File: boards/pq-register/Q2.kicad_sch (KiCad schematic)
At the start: 94 parts, among them Q100 MMBT5401, Q65 MMBT5401, Q73 MMBT5401, Q74 MMBT5401, Q75 MMBT5401, Q76 MMBT5401, Q77 MMBT5401, Q78 MMBT5401, Q79 MMBT5401, Q80 MMBT5401, Q81 MMBT5401, Q82 MMBT5401

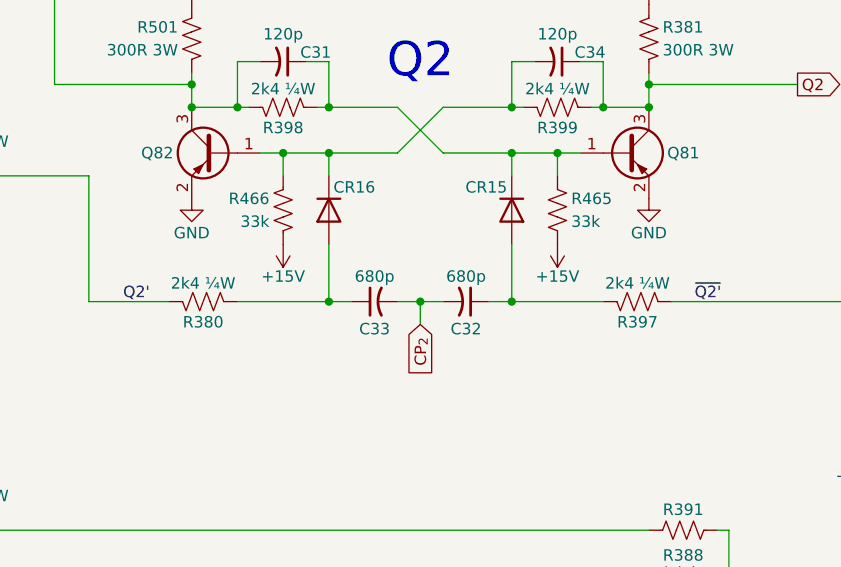
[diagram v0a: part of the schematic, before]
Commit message: Route resistors in the second column.
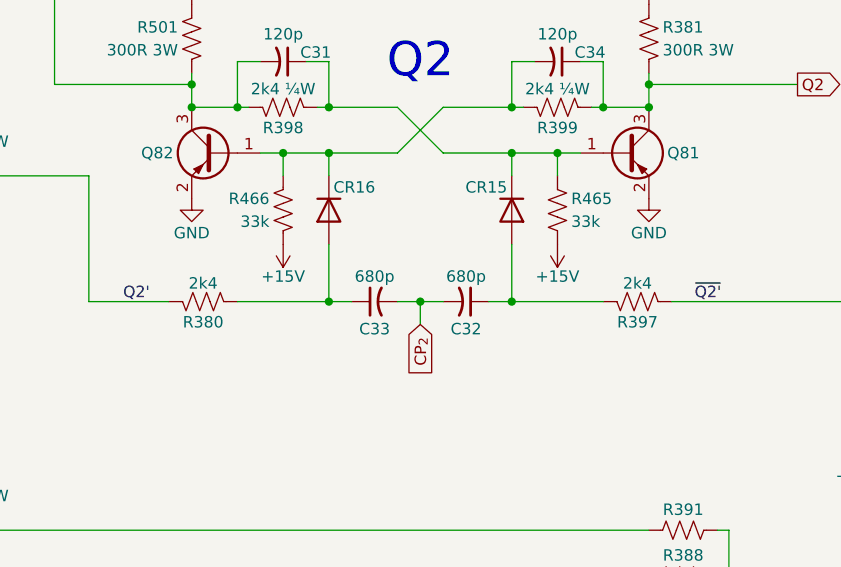
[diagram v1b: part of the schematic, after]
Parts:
- R380, R397: value 2k4 ¼W -> 2k4; footprint Resistor_SMD:R_0603_1608Metric -> Resistor_SMD:R_0402_1005Metric
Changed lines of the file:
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@@
 			)
 		)
-		(property "Value" "2k4 ¼W"
+		(property "Value" "2k4"
 			(at 176.53 61.468 90)
 			(show_name no)
@@
 			)
 		)
-		(property "Footprint" "Resistor_SMD:R_0603_1608Metric"
+		(property "Footprint" "Resistor_SMD:R_0402_1005Metric"
 			(at 176.784 64.516 90)
 			(hide yes)
@@
 			)
 		)
-		(property "Value" "2k4 ¼W"
+		(property "Value" "2k4"
 			(at 224.79 61.468 90)
 			(show_name no)
@@
 			)
 		)
-		(property "Footprint" "Resistor_SMD:R_0603_1608Metric"
+		(property "Footprint" "Resistor_SMD:R_0402_1005Metric"
 			(at 225.044 64.516 90)
 			(hide yes)

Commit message: Route passives in the rightmost column.
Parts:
- R903: renamed from R507; now fitted
- R904: renamed from R508; now fitted
- R906: renamed from R509; now fitted
- R907: renamed from R510; now fitted
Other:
- note removed: "Used 41 & up when IO Key, Data I/O, or A&D Converter boards are used. Works in normal not in 1op mode."
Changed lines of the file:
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@@
 		(comment 1 "https://github.com/Elemecca/lgp21-mini")
 	)
-	(text "Used 41 & up when IO Key,\nData I/O, or A&D Converter\nboards are used. Works in\nnormal not in 1op mode."
-		(exclude_from_sim no)
-		(at 116.078 30.226 0)
-		(effects
-			(font
-				(size 1.27 1.27)
-			)
-			(justify left)
-		)
-	)
 	(text "Q2"
 		(exclude_from_sim no)
@@
 		)
 	)
-	(polyline
-		(pts
-			(xy 118.11 44.45) (xy 118.11 45.72)
-		)
-		(stroke
-			(width 0)
-			(type default)
-		)
-	)
 	(wire
 		(pts
@@
 		)
 	)
-	(polyline
-		(pts
-			(xy 111.76 27.94) (xy 115.57 27.94)
-		)
-		(stroke
-			(width 0)
-			(type default)
-		)
-	)
 	(wire
 		(pts
@@
 		)
 	)
-	(polyline
-		(pts
-			(xy 118.11 44.45) (xy 118.11 45.72)
-		)
-		(stroke
-			(width 0)
-			(type default)
-		)
-	)
 	(wire
 		(pts
@@
 		)
 	)
-	(polyline
-		(pts
-			(xy 111.76 39.37) (xy 118.11 45.72)
-		)
-		(stroke
-			(width 0)
-			(type default)
-		)
-	)
 	(wire
 		(pts
@@
 		)
 	)
-	(polyline
-		(pts
-			(xy 111.76 27.94) (xy 111.76 39.37)
-		)
-		(stroke
-			(width 0)
-			(type default)
-		)
-	)
 	(wire
 		(pts
@@
 		)
 	)
-	(polyline
-		(pts
-			(xy 116.84 45.72) (xy 118.11 45.72)
-		)
-		(stroke
-			(width 0)
-			(type default)
-		)
-	)
 	(wire
 		(pts
@@
 		(on_board yes)
 		(in_pos_files yes)
-		(dnp yes)
-		(property "Reference" "R507"
+		(dnp no)
+		(property "Reference" "R903"
 			(at 74.93 49.784 90)
 			(show_name no)
@@
 			(project "pq-register"
 				(path "/d5da316c-1ec9-4d99-8330-1c4a3f6c3ba4/8256428c-4bd9-4db2-955d-d6beccbf8ae1"
-					(reference "R507")
+					(reference "R903")
 					(unit 1)
 				)
@@
 		(on_board yes)
 		(in_pos_files yes)
-		(dnp yes)
-		(property "Reference" "R510"
+		(dnp no)
+		(property "Reference" "R907"
 			(at 229.87 112.014 90)
 			(show_name no)
@@
 			(project "pq-register"
 				(path "/d5da316c-1ec9-4d99-8330-1c4a3f6c3ba4/8256428c-4bd9-4db2-955d-d6beccbf8ae1"
-					(reference "R510")
+					(reference "R907")
 					(unit 1)
 				)
@@
 		(on_board yes)
 		(in_pos_files yes)
-		(dnp yes)
-		(property "Reference" "R508"
+		(dnp no)
+		(property "Reference" "R904"
 			(at 128.27 45.974 90)
 			(show_name no)
@@
 			(project "pq-register"
 				(path "/d5da316c-1ec9-4d99-8330-1c4a3f6c3ba4/8256428c-4bd9-4db2-955d-d6beccbf8ae1"
-					(reference "R508")
+					(reference "R904")
 					(unit 1)
 				)
@@
 		(on_board yes)
 		(in_pos_files yes)
-		(dnp yes)
-		(property "Reference" "R509"
+		(dnp no)
+		(property "Reference" "R906"
 			(at 128.27 155.194 90)
 			(show_name no)
@@
 			(project "pq-register"
 				(path "/d5da316c-1ec9-4d99-8330-1c4a3f6c3ba4/8256428c-4bd9-4db2-955d-d6beccbf8ae1"
-					(reference "R509")
+					(reference "R906")
 					(unit 1)
 				)

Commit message: Assorted cleanup and silkscreen.
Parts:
- renumbered R906 to R902, R903 to R905, R904 to R906
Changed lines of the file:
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@@
 		(in_pos_files yes)
 		(dnp no)
-		(property "Reference" "R903"
+		(property "Reference" "R905"
 			(at 74.93 49.784 90)
 			(show_name no)
@@
 			(project "pq-register"
 				(path "/d5da316c-1ec9-4d99-8330-1c4a3f6c3ba4/8256428c-4bd9-4db2-955d-d6beccbf8ae1"
-					(reference "R903")
+					(reference "R905")
 					(unit 1)
 				)
@@
 		(in_pos_files yes)
 		(dnp no)
-		(property "Reference" "R904"
+		(property "Reference" "R906"
 			(at 128.27 45.974 90)
 			(show_name no)
@@
 			(project "pq-register"
 				(path "/d5da316c-1ec9-4d99-8330-1c4a3f6c3ba4/8256428c-4bd9-4db2-955d-d6beccbf8ae1"
-					(reference "R904")
+					(reference "R906")
 					(unit 1)
 				)
@@
 		(in_pos_files yes)
 		(dnp no)
-		(property "Reference" "R906"
+		(property "Reference" "R902"
 			(at 128.27 155.194 90)
 			(show_name no)
@@
 			(project "pq-register"
 				(path "/d5da316c-1ec9-4d99-8330-1c4a3f6c3ba4/8256428c-4bd9-4db2-955d-d6beccbf8ae1"
-					(reference "R906")
+					(reference "R902")
 					(unit 1)
 				)

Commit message: Add script to export production files.
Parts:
- C31, C34: BOM Value (none) -> 120pF
- C32, C33: BOM Value (none) -> 680pF
- CR15, CR16: value 1N5819WS -> 1N4148WS; BOM Value (none) -> 1N4148WS; LCSC (none) -> C2128
- Q100, Q65, Q73, Q74, Q75, Q76, Q77, Q78, Q79, Q80, Q81, Q82: BOM Value (none) -> MMBT5401; LCSC (none) -> C8326
- R285, R299, R301, R303, R305, R457, R459, R461, R463, R497: BOM Value (none) -> 56kΩ
- R286, R300, R302, R304, R306, R458, R460, R462, R464, R498: BOM Value (none) -> 2kΩ 500mW
- R343, R344, R345, R346, R347, R348, R349, R365, R366, R367, R368, R369, R370, R371, R372, R373, R374, R375, R376, R377, R378, R379, R384, R385, R386, R387, R388, R389, R390, R391, R392, R393, R394, R395, R396, R448, R449, R450, R451, R452, R453, R454, R455, R456, R902, R905, R906, R907: BOM Value (none) -> 15kΩ
- R380, R397: BOM Value (none) -> 2.4kΩ
- R381, R501: BOM Value (none) -> 300Ω 3W
- R398, R399: BOM Value (none) -> 2.4kΩ 250mW
- R465, R466: BOM Value (none) -> 33kΩ
